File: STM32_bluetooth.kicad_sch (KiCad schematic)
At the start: 41 parts, among them J1 USB_C_Receptacle_USB2.0_16P, J2 Conn_01x04_Pin, J3 Conn_ARM_SWD_TagConnect_TC2030, J4 Conn_Coaxial, SW1 SW_Push, U1 MIC5365-3.3YD5, U2 USBLC6-2SC6, U3 STM32WB55CEU6, X1 32kHz768, X2 32MHz

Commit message: Added all footprints
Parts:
- C1, C5: value C -> 4u7; footprint (none) -> Capacitor_SMD:C_0402_1005Metric
- C10, C11, C12, C14, C17, C18, C19, C3, C4, C6, C7, C8, R1, R2, R3, R4, R5, R6, R7: footprint (none) -> Capacitor_SMD:C_0402_1005Metric
- C13, C15: value C -> 10p; footprint (none) -> Capacitor_SMD:C_0402_1005Metric
- C16, C2, C9: footprint (none) -> Capacitor_SMD:C_0603_1608Metric
- D1: footprint (none) -> LED_SMD:LED_0402_1005Metric
- J1: footprint (none) -> Connector_USB:USB_C_Receptacle_GCT_USB4105-xx-A_16P_TopMnt_Horizontal
- J2: footprint (none) -> Connector_Molex:Molex_PicoBlade_53048-0410_1x04_P1.25mm_Horizontal
- J4: footprint (none) -> Connector_Coaxial:U.FL_Hirose_U.FL-R-SMT-1_Vertical
- L1, L3: footprint (none) -> Inductor_SMD:L_0402_1005Metric
- L2: footprint (none) -> Inductor_SMD:L_0805_2012Metric
- SW1: footprint (none) -> Button_Switch_SMD:SW_SPST_CK_RS282G05A3
- X1: footprint (none) -> Crystal:Crystal_SMD_2012-2Pin_2.0x1.2mm
- X2: footprint (none) -> Crystal:Crystal_SMD_2016-4Pin_2.0x1.6mm
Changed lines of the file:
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@@
 			)
 		)
-		(property "Footprint" ""
+		(property "Footprint" "Capacitor_SMD:C_0603_1608Metric"
 			(at 110.1852 43.18 0)
 			(effects
@@
 			)
 		)
-		(property "Footprint" ""
+		(property "Footprint" "Capacitor_SMD:C_0402_1005Metric"
 			(at 63.1952 62.23 0)
 			(effects
@@
 			)
 		)
-		(property "Value" "C"
+		(property "Value" "4u7"
 			(at 34.29 30.4799 0)
 			(effects
@@
 			)
 		)
-		(property "Footprint" ""
+		(property "Footprint" "Capacitor_SMD:C_0402_1005Metric"
 			(at 31.4452 33.02 0)
 			(effects
@@
 			)
 		)
-		(property "Footprint" ""
+		(property "Footprint" "Capacitor_SMD:C_0402_1005Metric"
 			(at 178.7652 66.04 0)
 			(effects
@@
 			)
 		)
-		(property "Footprint" ""
+		(property "Footprint" "Connector_USB:USB_C_Receptacle_GCT_USB4105-xx-A_16P_TopMnt_Horizontal"
 			(at 41.91 96.52 0)
 			(effects
@@
 			)
 		)
-		(property "Value" "C"
+		(property "Value" "10p"
 			(at 166.37 132.0799 0)
 			(effects
@@
 			)
 		)
-		(property "Footprint" ""
+		(property "Footprint" "Capacitor_SMD:C_0402_1005Metric"
 			(at 163.5252 134.62 0)
 			(effects
@@
 			)
 		)
-		(property "Footprint" ""
+		(property "Footprint" "Capacitor_SMD:C_0402_1005Metric"
 			(at 86.0552 62.23 0)
 			(effects
@@
 			)
 		)
-		(property "Footprint" ""
+		(property "Footprint" "LED_SMD:LED_0402_1005Metric"
 			(at 110.49 91.44 0)
 			(effects
@@
 			)
 		)
-		(property "Footprint" ""
+		(property "Footprint" "Capacitor_SMD:C_0603_1608Metric"
 			(at 51.7652 62.23 0)
 			(effects
@@
 			)
 		)
-		(property "Footprint" ""
+		(property "Footprint" "Capacitor_SMD:C_0402_1005Metric"
 			(at 120.3452 62.23 0)
 			(effects
@@
 			)
 		)
-		(property "Footprint" ""
+		(property "Footprint" "Capacitor_SMD:C_0402_1005Metric"
 			(at 100.33 93.218 90)
 			(effects
@@
 			)
 		)
-		(property "Footprint" ""
+		(property "Footprint" "Capacitor_SMD:C_0402_1005Metric"
 			(at 213.0552 106.68 0)
 			(effects
@@
 			)
 		)
-		(property "Footprint" ""
+		(property "Footprint" "Capacitor_SMD:C_0603_1608Metric"
 			(at 195.2752 87.63 0)
 			(effects
@@
 			)
 		)
-		(property "Footprint" ""
+		(property "Footprint" "Connector_Coaxial:U.FL_Hirose_U.FL-R-SMT-1_Vertical"
 			(at 264.16 96.52 0)
 			(effects
@@
 			)
 		)
-		(property "Footprint" ""
+		(property "Footprint" "Capacitor_SMD:C_0402_1005Metric"
 			(at 241.3 132.588 90)
 			(effects
@@
 			)
 		)
-		(property "Footprint" ""
+		(property "Footprint" "Crystal:Crystal_SMD_2016-4Pin_2.0x1.6mm"
 			(at 194.31 124.46 0)
 			(effects
@@
 			)
 		)
-		(property "Footprint" ""
+		(property "Footprint" "Capacitor_SMD:C_0402_1005Metric"
 			(at 225.7552 106.68 0)
 			(effects
@@
 			)
 		)
-		(property "Footprint" ""
+		(property "Footprint" "Inductor_SMD:L_0805_2012Metric"
 			(at 181.61 78.74 0)
 			(effects
@@
 			)
 		)
-		(property "Footprint" ""
+		(property "Footprint" "Capacitor_SMD:C_0402_1005Metric"
 			(at 97.79 80.518 90)
 			(effects
@@
 			)
 		)
-		(property "Footprint" ""
+		(property "Footprint" "Capacitor_SMD:C_0402_1005Metric"
 			(at 74.6252 62.23 0)
 			(effects
@@
 			)
 		)
-		(property "Footprint" ""
+		(property "Footprint" "Button_Switch_SMD:SW_SPST_CK_RS282G05A3"
 			(at 257.81 125.73 0)
 			(effects
@@
 			)
 		)
-		(property "Footprint" ""
+		(property "Footprint" "Capacitor_SMD:C_0402_1005Metric"
 			(at 121.6152 43.18 0)
 			(effects
@@
 			)
 		)
-		(property "Footprint" ""
+		(property "Footprint" "Inductor_SMD:L_0402_1005Metric"
 			(at 168.91 78.74 0)
 			(effects
@@
 			)
 		)
-		(property "Footprint" ""
+		(property "Footprint" "Capacitor_SMD:C_0402_1005Metric"
 			(at 97.79 83.058 90)
 			(effects
@@
 			)
 		)
-		(property "Footprint" ""
+		(property "Footprint" "Crystal:Crystal_SMD_2012-2Pin_2.0x1.2mm"
 			(at 170.18 120.65 0)
 			(effects
@@
 			)
 		)
-		(property "Footprint" ""
+		(property "Footprint" "Capacitor_SMD:C_0402_1005Metric"
 			(at 65.278 118.11 90)
 			(effects
@@
 			)
 		)
-		(property "Footprint" ""
+		(property "Footprint" "Capacitor_SMD:C_0402_1005Metric"
 			(at 57.912 118.11 90)
 			(effects
@@
 			)
 		)
-		(property "Value" "C"
+		(property "Value" "10p"
 			(at 178.308 133.096 0)
 			(effects
@@
 			)
 		)
-		(property "Footprint" ""
+		(property "Footprint" "Capacitor_SMD:C_0402_1005Metric"
 			(at 178.7652 134.62 0)
 			(effects
@@
 			)
 		)
-		(property "Footprint" ""
+		(property "Footprint" "Capacitor_SMD:C_0402_1005Metric"
 			(at 145.7452 43.18 0)
 			(effects
@@
 			)
 		)
-		(property "Footprint" ""
+		(property "Footprint" "Capacitor_SMD:C_0402_1005Metric"
 			(at 97.4852 62.23 0)
 			(effects
@@
 			)
 		)
-		(property "Footprint" ""
+		(property "Footprint" "Capacitor_SMD:C_0402_1005Metric"
 			(at 108.9152 62.23 0)
 			(effects
@@
 			)
 		)
-		(property "Footprint" ""
+		(property "Footprint" "Inductor_SMD:L_0402_1005Metric"
 			(at 218.44 96.52 0)
 			(effects
@@
 			)
 		)
-		(property "Value" "C"
+		(property "Value" "4u7"
 			(at 80.01 31.7499 0)
 			(effects
@@
 			)
 		)
-		(property "Footprint" ""
+		(property "Footprint" "Capacitor_SMD:C_0402_1005Metric"
 			(at 77.1652 34.29 0)
 			(effects
@@
 			)
 		)
-		(property "Footprint" ""
+		(property "Footprint" "Connector_Molex:Molex_PicoBlade_53048-0410_1x04_P1.25mm_Horizontal"
 			(at 78.74 78.74 0)
 			(effects
@@
 			)
 		)
-		(property "Footprint" ""
+		(property "Footprint" "Capacitor_SMD:C_0402_1005Metric"
 			(at 210.312 137.16 90)
 			(effects
@@
 			)
 		)
-		(property "Footprint" ""
+		(property "Footprint" "Capacitor_SMD:C_0402_1005Metric"
 			(at 227.0252 140.97 0)
 			(effects

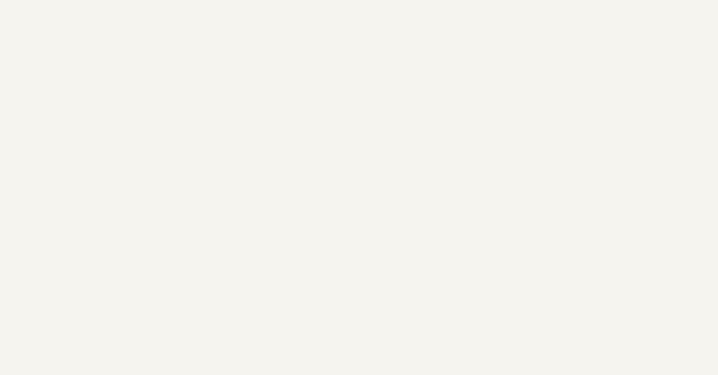
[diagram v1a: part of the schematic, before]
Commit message: Added via's and tracing for RF circuit.
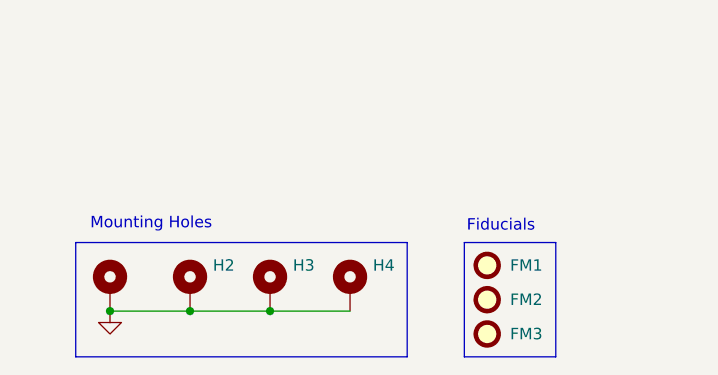
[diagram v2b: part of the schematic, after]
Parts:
- added FM1, FM2, FM3: Fiducial, Fiducial:Fiducial_1mm_Mask2mm, symbol Mechanical:Fiducial
- added H1, H2, H3, H4: MountingHole_Pad, MountingHole:MountingHole_2.2mm_M2_Pad_Via, symbol Mechanical:MountingHole_Pad
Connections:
- net GND: now also H1.1, H2.1, H3.1, H4.1
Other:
- note added: "Fiducials"
- note added: "Mounting Holes"
